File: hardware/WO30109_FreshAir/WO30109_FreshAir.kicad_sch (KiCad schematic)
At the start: 59 parts, among them K1 G5Q-1 DC12, K2 G5Q-1 DC12, K3 G5Q-1 DC12, K4 G5Q-1 DC12, P1 AC IN 230V, P2 PROG, P3 AC OUT, Q1 Si2302CDS, Q2 Si2302CDS, Q3 Si2302CDS, Q4 Si2302CDS, U1 ESP32-C6-WROOM-1-N8, U2 IRM-02-12, U3 SYN480R, U4 AP63203WU-7, Y1 13.52127MHz 20pF

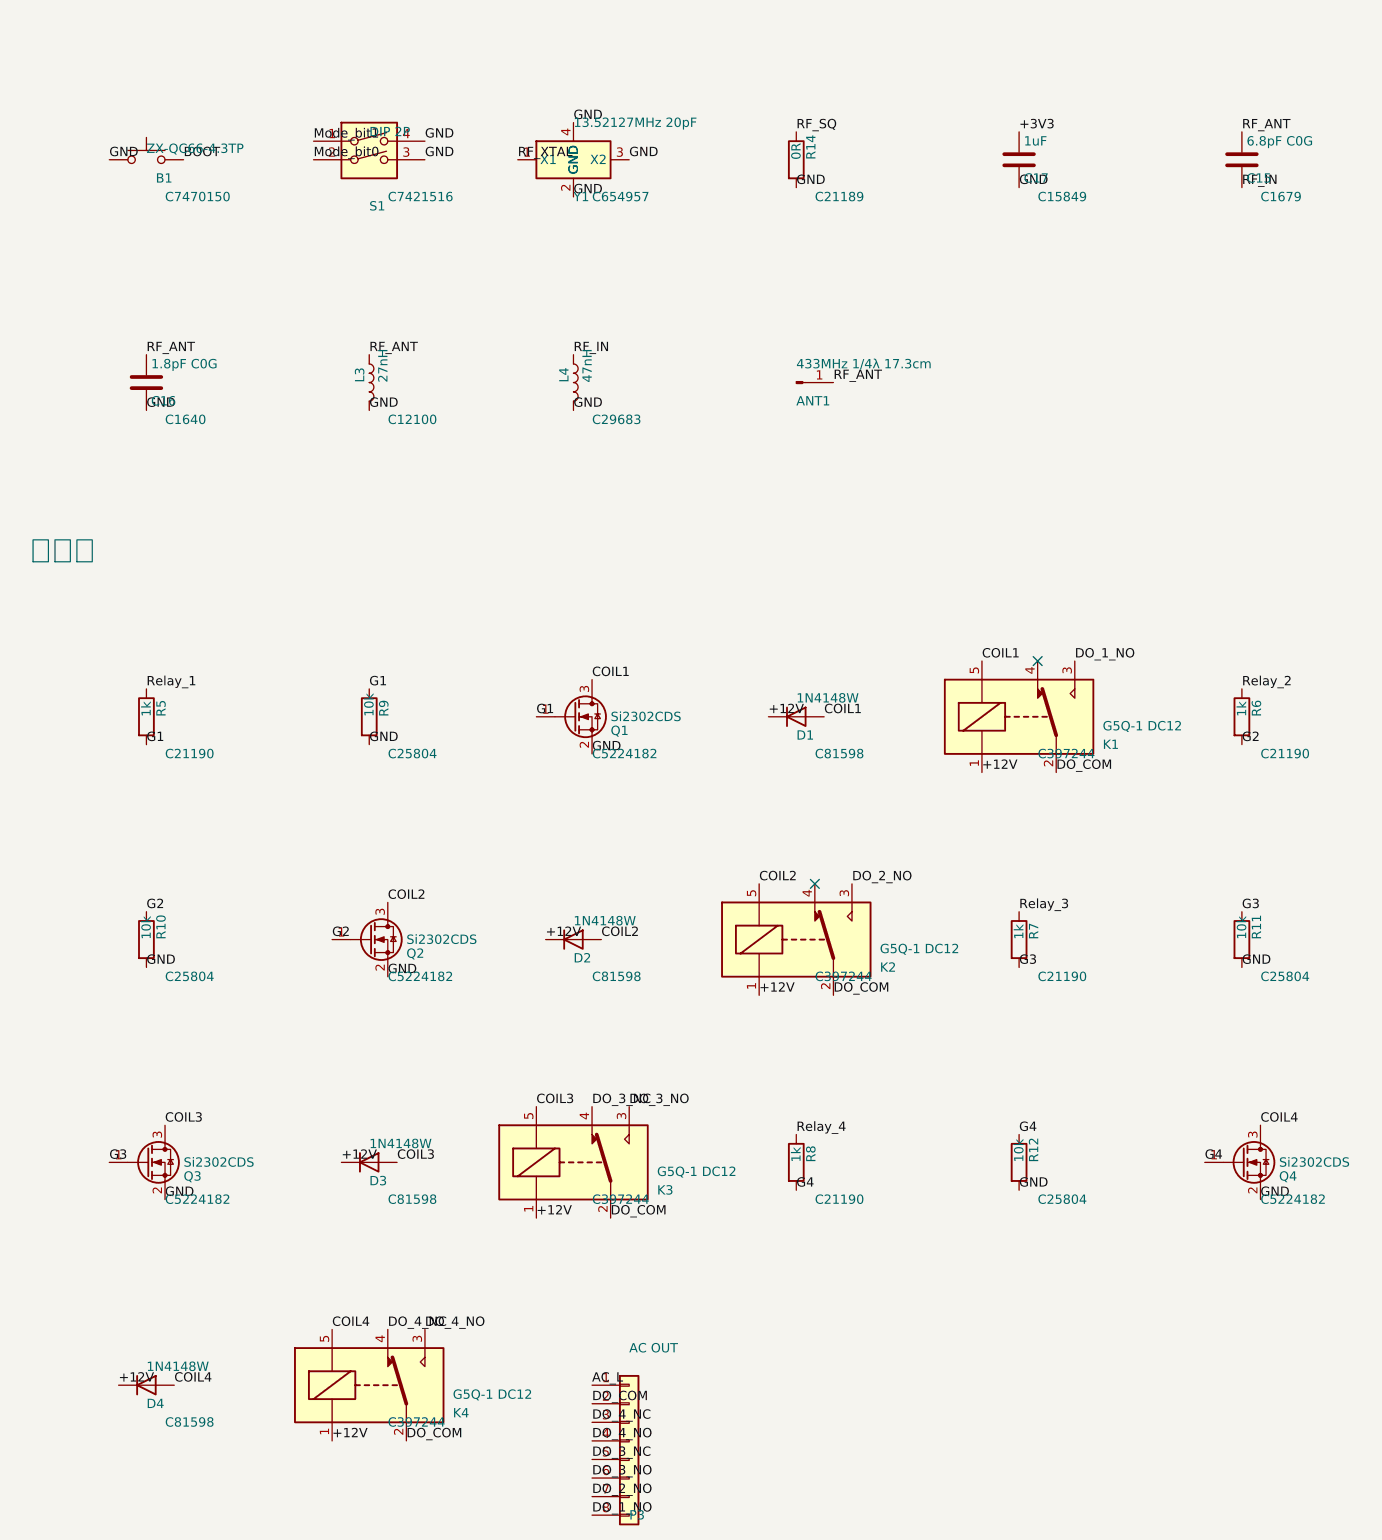
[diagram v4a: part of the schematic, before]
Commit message: hw: V3.1 433 匹配重新選值、續流改 B5819W（只換值不改佈線）
- C15/C16 2.7pF（C162221）、L3 47nH（C29683）、L4 33nH（C35050）：規格書值以同系列
  Micrel 原廠輸入阻抗算峰值在 210–230MHz，新值 433.92MHz 失配 8–13dB → 3.1–5.3dB
- D1–D4 1N4148W → B5819W（C8598，基礎料、同 SOD-123），配合 PWM 保持（Vf ≤0.4V）
- sim/rf_match.cir 改用原廠阻抗、新舊值並排；scripts/rf_match_opt.py 最差情況選值
- jlc_footprints.json 補新料號、刪舊料號；--refresh-footprints 預設只抓缺的
- ERC 0、DRC 0、parity 0

Co-Authored-By: Claude Opus 5.5 (1M context) <noreply@anthropic.com>
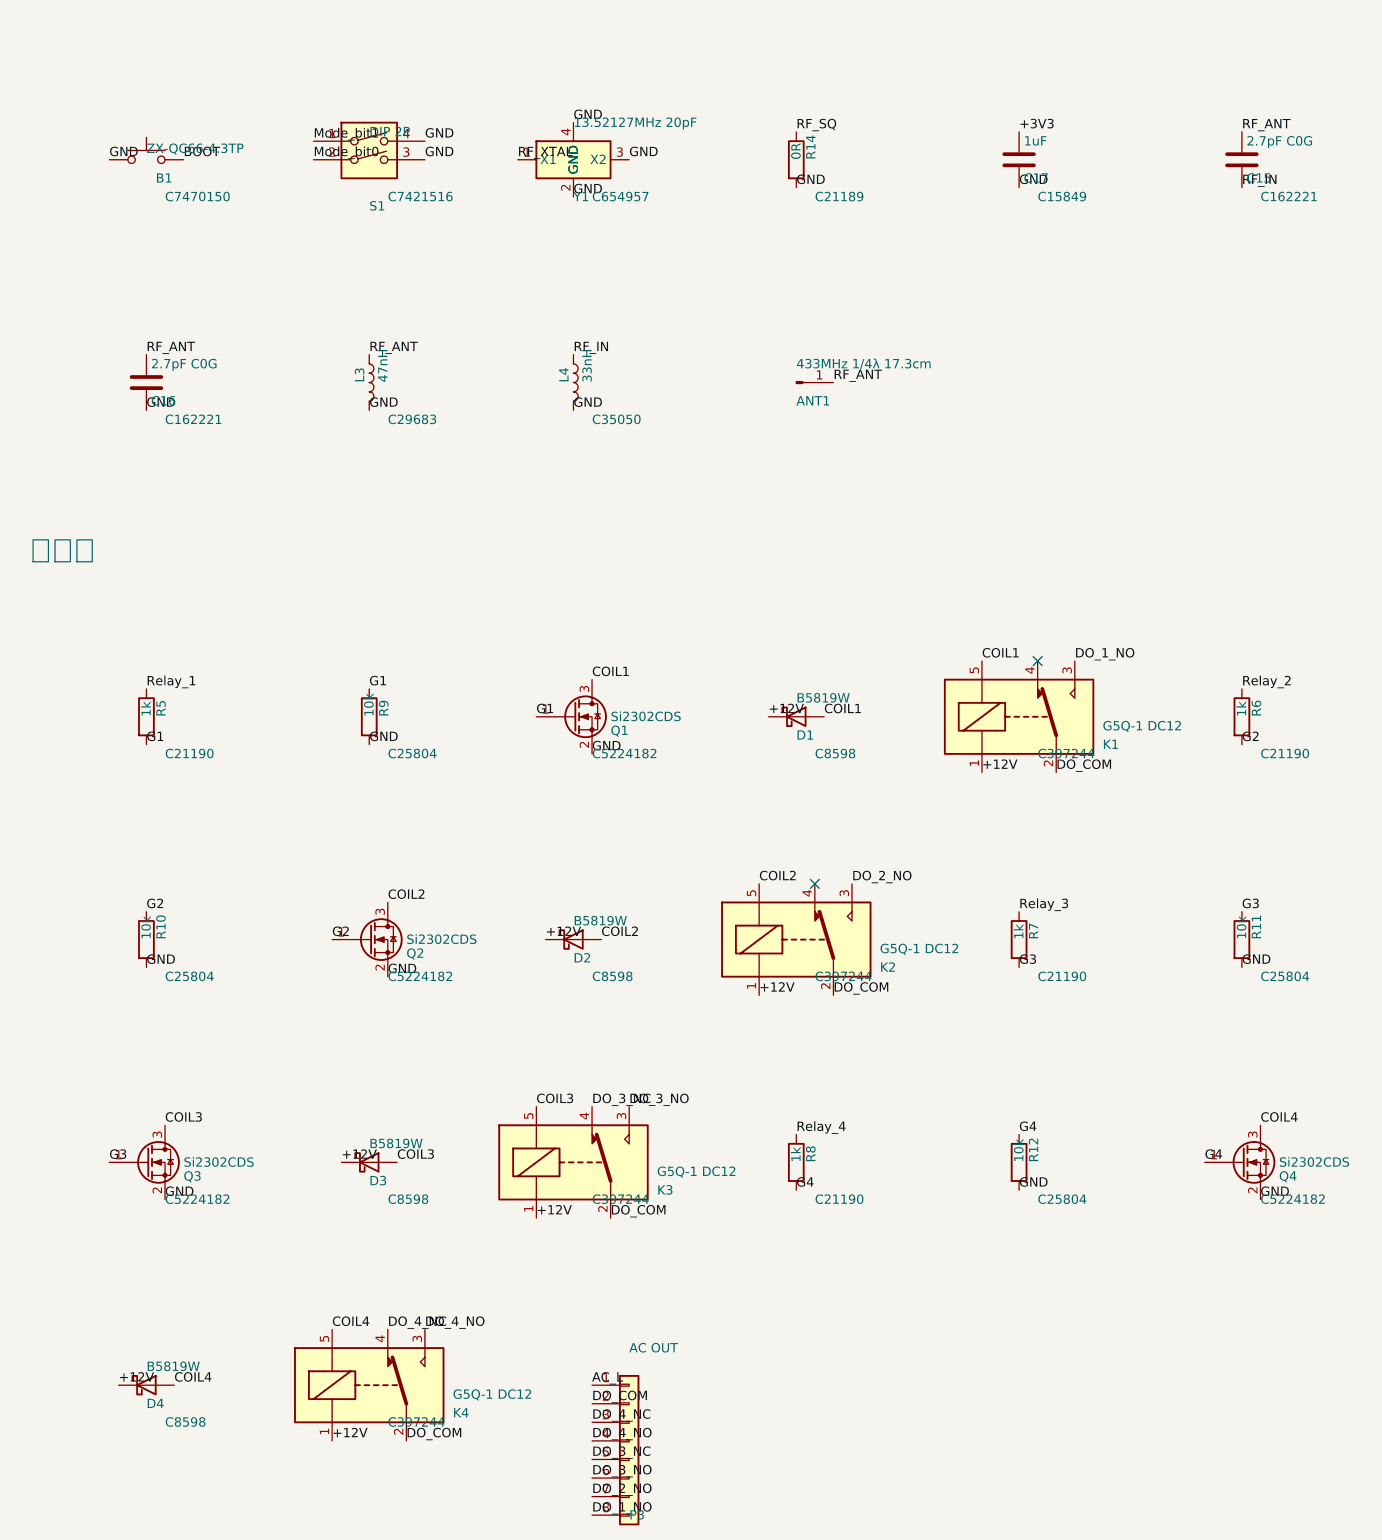
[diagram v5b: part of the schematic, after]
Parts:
- removed D1, D2, D3, D4: 1N4148W, Diode_SMD:D_SOD-123, symbol Diode:1N4148W
- added D1, D2, D3, D4: B5819W, Diode_SMD:D_SOD-123, symbol Device:D_Schottky
- C15: value 6.8pF C0G -> 2.7pF C0G; LCSC C1679 -> C162221
- C16: value 1.8pF C0G -> 2.7pF C0G; LCSC C1640 -> C162221
- L3: value 27nH -> 47nH; LCSC C12100 -> C29683
- L4: value 47nH -> 33nH; LCSC C29683 -> C35050
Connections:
- net +12V: now also D1.1 (K), D2.1 (K), D3.1 (K), D4.1 (K)
- net COIL1: now also D1.2 (A)
- net COIL2: now also D2.2 (A)
- net COIL3: now also D3.2 (A)
- net COIL4: now also D4.2 (A)

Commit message: hw: V3.2 4 路光耦 DI 輸入、拿掉指撥，上緣加長 10mm
- J5 7P 3.5mm 插拔端子：+12V（R23 1.5k 限流，短路 8mA）／IN1–IN4／COM／GND
- U5 TLP290-4 交流輸入光耦 ×4（乾接點、5–24VDC、NPN/PNP 都可），R15–R18 3.3k，C18–C21 10nF
- DI1–4 → IO22/IO21/IO20/IO19（內建上拉）；S1 指撥拿掉
- scripts/upgrade_v32_pcb.py：從 V3.1 PCB 重建，A* 佈新網路（不動既有走線、繞開 433 匹配區、
  長線自動試佈線順序、新區域縫合與孤島接回）
- mains_router：stamp_r、keep_cl、封裝內建禁佈區、set_board（預設值維持舊行為）
- add_stitching：STITCH_REGION、--islands；assign_3d 冪等；7P 端子封裝與 3D 模型
- ERC 0；DRC 錯誤 0、未連線 0、parity 0；CPL 測試 OK

Co-Authored-By: Claude Opus 5.5 (1M context) <noreply@anthropic.com>
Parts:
- removed S1: DIP 2P, Button_Switch_SMD:SW_DIP_SPSTx02_Slide_Copal_CHS-02B_W7.62mm_P1.27mm, symbol Switch:SW_DIP_x02
- added C18, C19, C20, C21: 10nF, Capacitor_SMD:C_0603_1608Metric, symbol Device:C
- added J5: DI 12V/IN1-4/COM/GND, WOOW:TerminalBlock_Pluggable_1x07_P3.50mm_Horizontal, symbol Connector_Generic:Conn_01x07
- added R15, R16, R17, R18: 3.3k, Resistor_SMD:R_1206_3216Metric, symbol Device:R
- added R23: 1.5k, Resistor_SMD:R_1206_3216Metric, symbol Device:R
- added U5: TLP290-4, Package_SO:SOP-16_4.55x10.3mm_P1.27mm, symbol WOOW:TLP290-4
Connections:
- net +12V: now also R23.1
- net GND: now also C18.2, C19.2, C20.2, C21.2, J5.7 (Pin_7), U5.11 (E3), U5.13 (E2), U5.15 (E1), U5.9 (E4)
- net DI_4: now reaches U1.17 (IO19)
- net DI_4: now also C21.1, U5.10 (C4)
- net DI_3: now reaches U1.18 (IO20)
- net DI_3: now also C20.1, U5.12 (C3)
- net DI_2: now reaches U1.19 (IO21)
- net DI_2: now also C19.1, U5.14 (C2)
- net DI_1: now reaches U1.20 (IO22)
- net DI_1: now also C18.1, U5.16 (C1)
- net Mode_bit0: no longer names the net of U1.11 (IO10)
- net Mode_bit1: no longer names the net of U1.12 (IO11)
- new net +12V_DI: J5.1 (Pin_1), R23.2
- new net DI_A1: R15.2, U5.1 (A1)
- new net DI_A2: R16.2, U5.3 (A2)
- new net DI_A3: R17.2, U5.5 (A3)
- new net DI_A4: R18.2, U5.7 (A4)
- new net DI_COM: J5.6 (Pin_6), U5.2 (K1), U5.4 (K2), U5.6 (K3), U5.8 (K4)
- new net DI_IN1: J5.2 (Pin_2), R15.1
- new net DI_IN2: J5.3 (Pin_3), R16.1
- new net DI_IN3: J5.4 (Pin_4), R17.1
- new net DI_IN4: J5.5 (Pin_5), R18.1
- no-connect marks 15 -> 13
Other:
- note added: "DI 輸入（光耦隔離）"

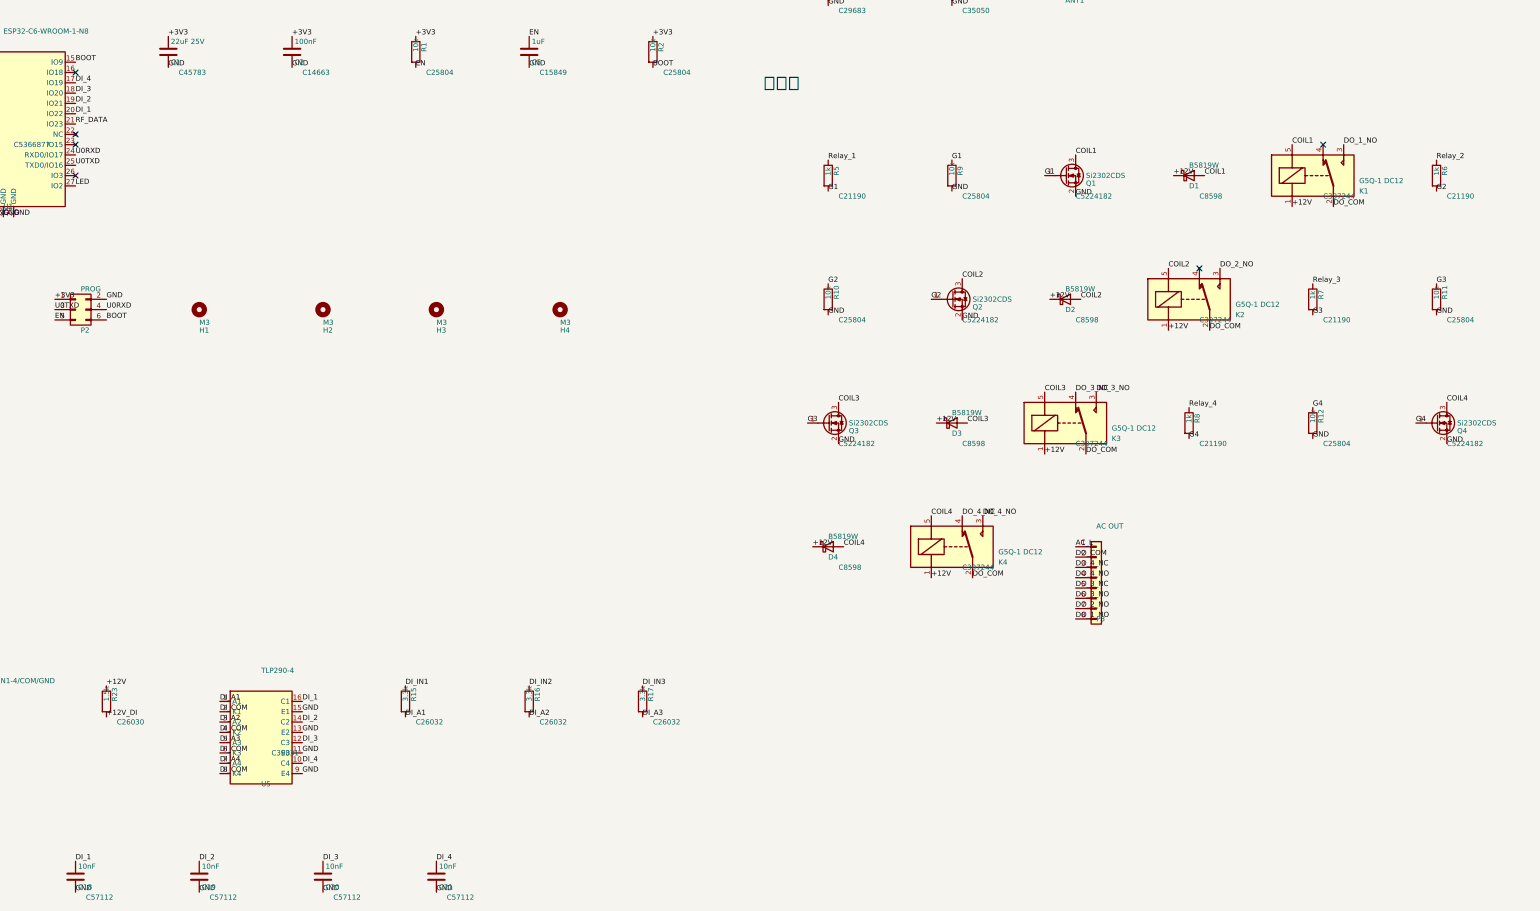
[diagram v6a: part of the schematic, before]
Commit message: hw: V3.3 NFC 設定介面（ST25DV04KC＋板上印刷線圈），J5 改到左側板邊
- U6 ST25DV04KC（C3304276，ISO 15693＋I2C）；L5 板上線圈 14.9×14.6mm 8 圈 1.277µH，
  C22 75pF（C1681）→ 13.84MHz，C24 微調空位；I2C SDA=IO20、SCL=IO19，10k 上拉
- DI_1–4 改接 IO3/IO15/IO22/IO21（與 I2C 照左右順序排，佈線不交叉）
- J5 直立貼左側板邊，左半段上緣到 107.2mm，左上角給線圈
- upgrade_v32_pcb.py 以 WO_VER=3.2／3.3 切換；nfc_coil.py 以實際封裝銅箔算電感
- mains_router：禁布區外擴半線寬、禁止鋪銅的禁布區也擋、讀真實 L 形板框
- add_stitching --prune 也移除懸空 GND 過孔
- ERC 0；DRC 錯誤 0、未連線 0、parity 0；V3.2 用新程式重建仍為 0

Co-Authored-By: Claude Opus 5.5 (1M context) <noreply@anthropic.com>
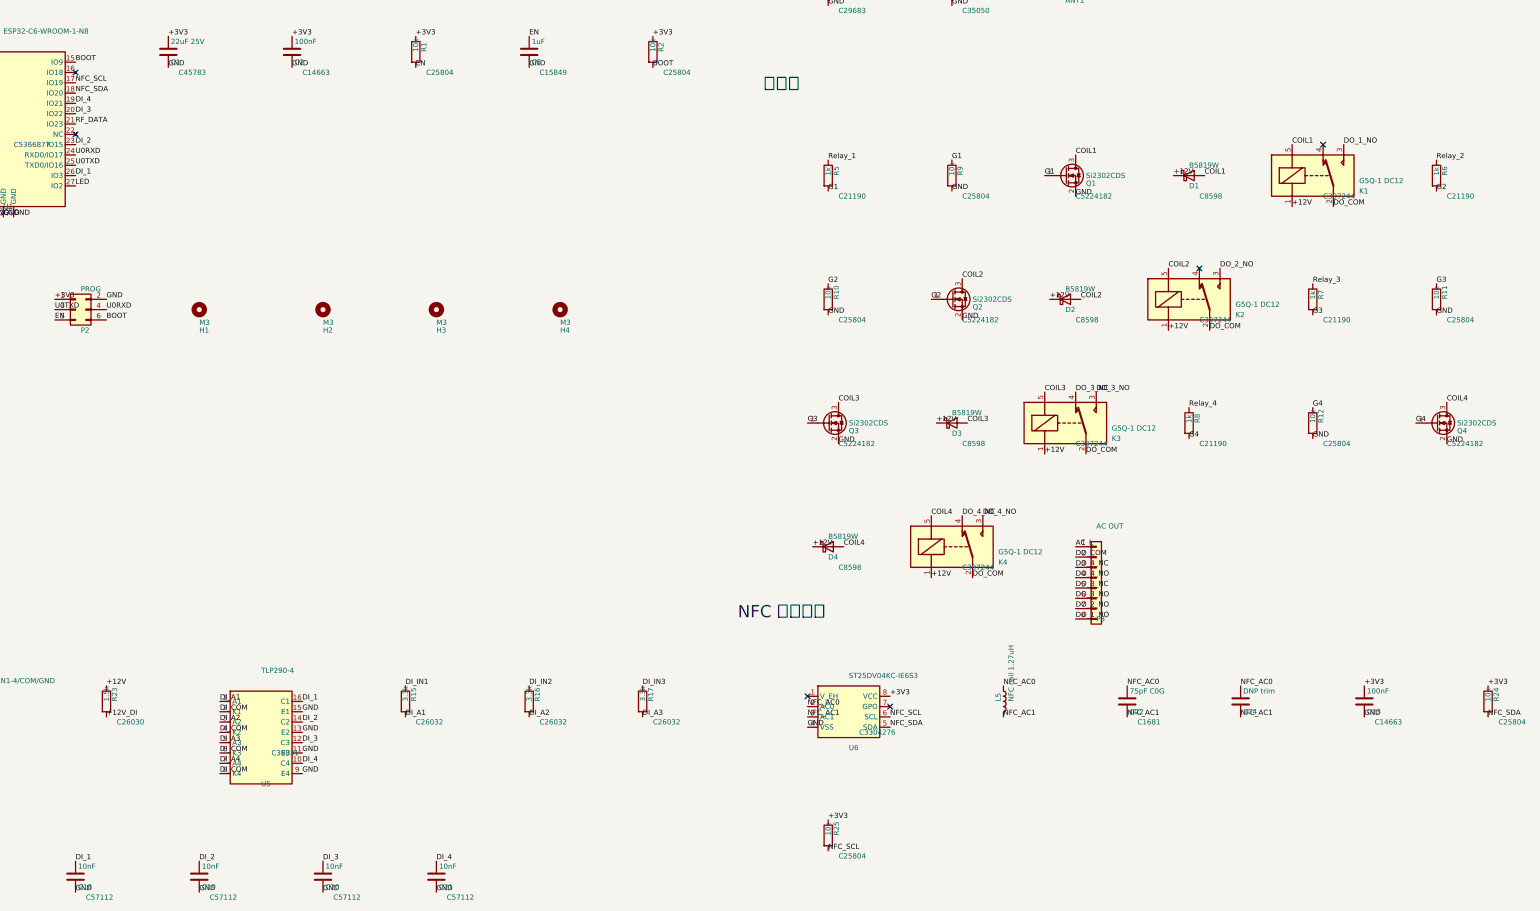
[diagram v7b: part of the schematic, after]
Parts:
- added C22: 75pF C0G, Capacitor_SMD:C_0603_1608Metric, symbol Device:C
- added C23: 100nF, Capacitor_SMD:C_0603_1608Metric, symbol Device:C
- added C24: DNP trim, Capacitor_SMD:C_0603_1608Metric, symbol Device:C
- added L5: NFC coil 1.27uH, WOOW:NFC_Coil_14.9x14.6mm_8T, symbol Device:L
- added R24, R25: 10k, Resistor_SMD:R_0603_1608Metric, symbol Device:R
- added U6: ST25DV04KC-IE6S3, Package_SO:SOIC-8_3.9x4.9mm_P1.27mm, symbol WOOW:ST25DV04KC
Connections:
- net +3V3: now also C23.1, R24.1, R25.1, U6.8 (VCC)
- net DI_1: now also U1.26 (IO3); no longer U1.20 (IO22)
- net DI_2: now also U1.23 (IO15); no longer U1.19 (IO21)
- net DI_3: now also U1.20 (IO22); no longer U1.18 (IO20)
- net DI_4: now also U1.19 (IO21); no longer U1.17 (IO19)
- net GND: now also C23.2, U6.4 (VSS)
- new net NFC_AC0: C22.1, C24.1, L5.1, U6.2 (AC0)
- new net NFC_AC1: C22.2, C24.2, L5.2, U6.3 (AC1)
- new net NFC_SCL: R25.2, U1.17 (IO19), U6.6 (SCL)
- new net NFC_SDA: R24.2, U1.18 (IO20), U6.5 (SDA)
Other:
- note added: "NFC 設定介面"
